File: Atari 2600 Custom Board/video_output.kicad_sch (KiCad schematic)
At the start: 0 parts

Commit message: Added buffer symbol and foot print
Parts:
- added U2: CD74HC4050M96, D16, symbol Atari2600_Library:CD74HC4050M96
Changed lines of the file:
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@@
 	(generator_version "8.0")
 	(paper "A4")
+	(symbol
+		(lib_id "Atari2600_Library:CD74HC4050M96")
+		(at 81.28 92.71 0)
+		(unit 1)
+		(exclude_from_sim no)
+		(in_bom yes)
+		(on_board yes)
+		(dnp no)
+		(fields_autoplaced yes)
+		(property "Reference" "U2"
+			(at 109.22 82.55 0)
+			(effects
+				(font
+					(size 1.524 1.524)
+				)
+			)
+		)
+		(property "Value" "CD74HC4050M96"
+			(at 109.22 85.09 0)
+			(effects
+				(font
+					(size 1.524 1.524)
+				)
+			)
+		)
+		(property "Footprint" "D16"
+			(at 81.28 92.71 0)
+			(effects
+				(font
+					(size 1.27 1.27)
+					(italic yes)
+				)
+				(hide yes)
+			)
+		)
+		(property "Datasheet" "CD74HC4050M96"
+			(at 81.28 92.71 0)
+			(effects
+				(font
+					(size 1.27 1.27)
+					(italic yes)
+				)
+				(hide yes)
+			)
+		)
+		(property "Description" ""
+			(at 81.28 92.71 0)
+			(effects
+				(font
+					(size 1.27 1.27)
+				)
+				(hide yes)
+			)
+		)
+		(pin "16"
+		)
+		(pin "15"
+		)
+		(pin "2"
+		)
+		(pin "12"
+		)
+		(pin "6"
+		)
+		(pin "8"
+		)
+		(pin "9"
+		)
+		(pin "4"
+		)
+		(pin "10"
+		)
+		(pin "14"
+		)
+		(pin "5"
+		)
+		(pin "7"
+		)
+		(pin "11"
+		)
+		(pin "1"
+		)
+		(pin "13"
+		)
+		(pin "3"
+		)
+		(instances
+			(project "atari2600"
+				(path "/d26a1e82-f8cb-48a3-8cce-edbb66ba228a/9cf3e399-02a1-4fa7-a3f8-062a21609052"
+					(reference "U2")
+					(unit 1)
+				)
+			)
+		)
+	)
 )

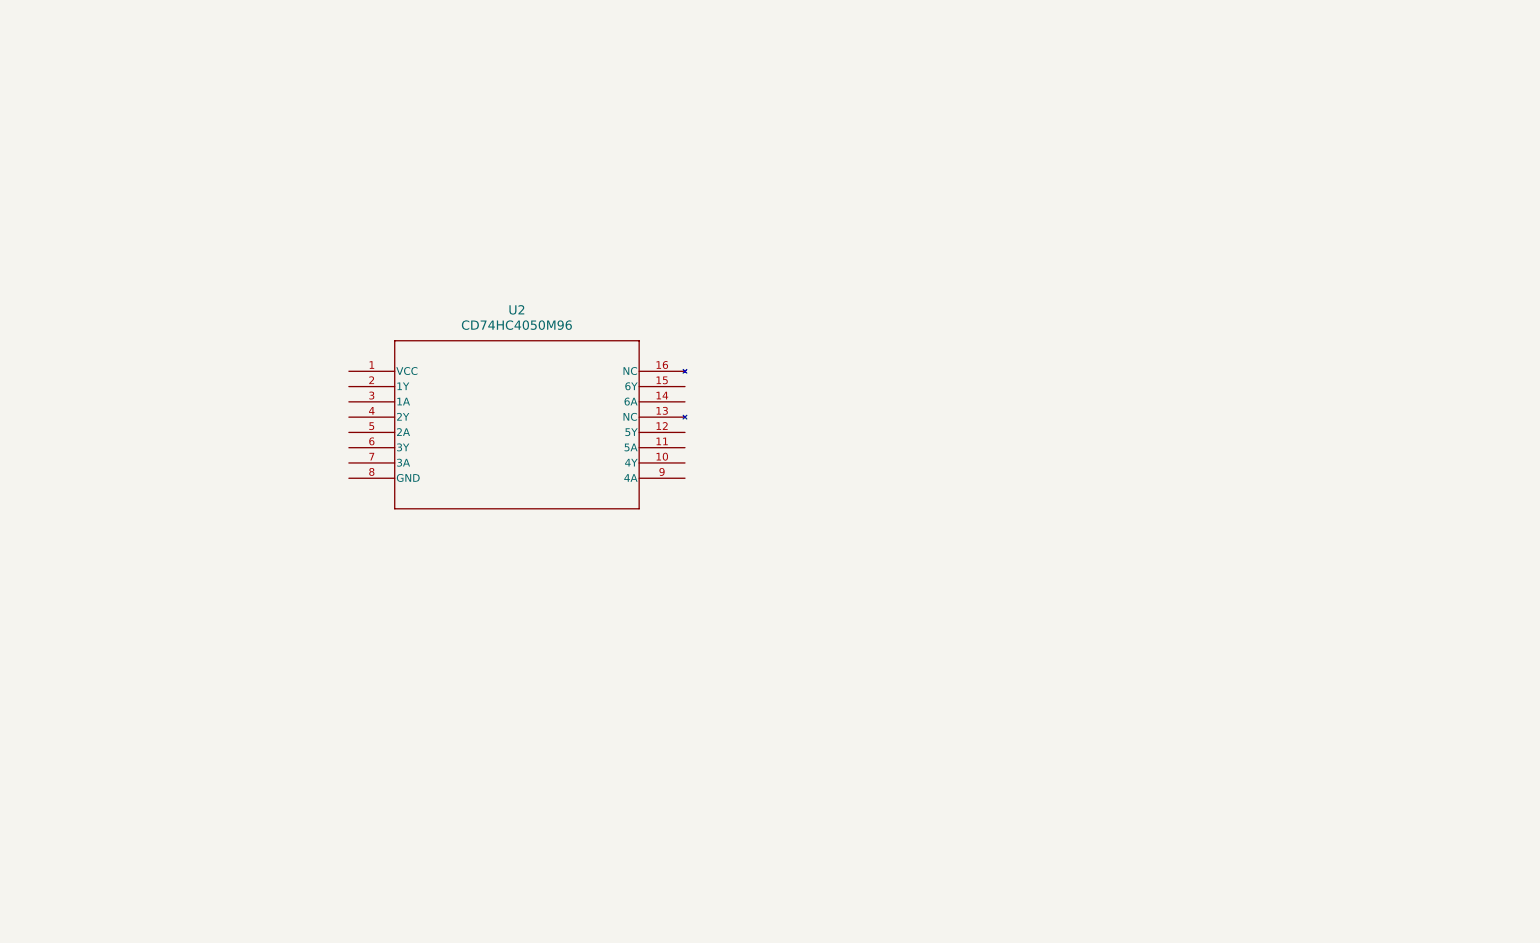
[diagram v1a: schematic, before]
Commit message: 1st pass of full schematic
1st pass of full schematic.  Need rules check and review.
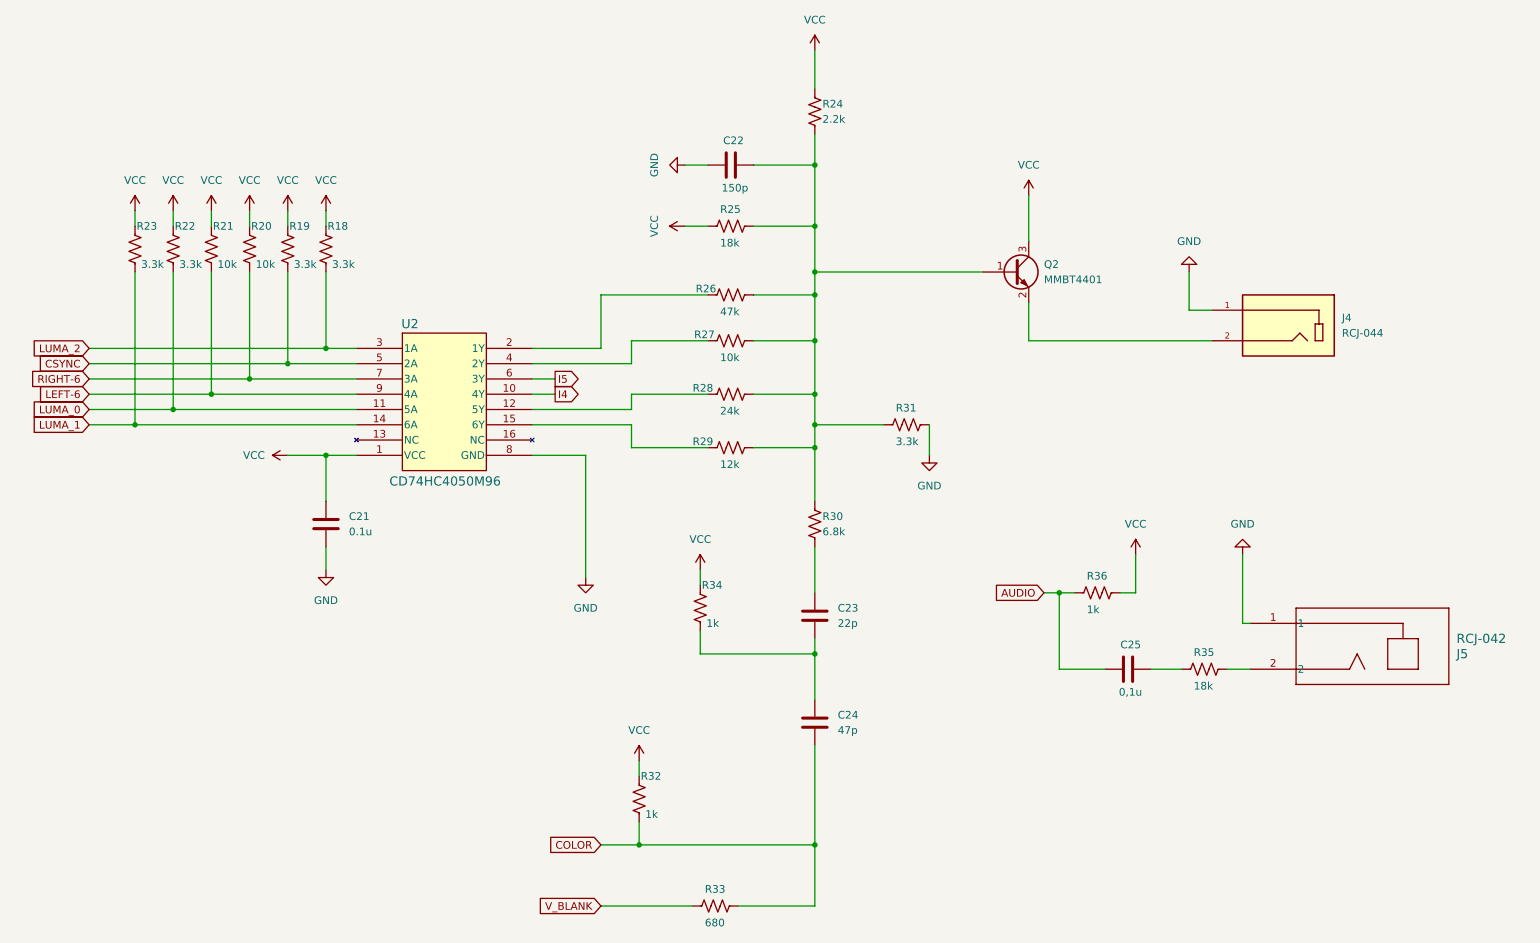
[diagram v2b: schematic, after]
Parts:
- added C21: 0.1u, symbol Device:C
- added C22: 150p, symbol Device:C
- added C23: 22p, symbol Device:C
- added C24: 47p, symbol Device:C
- added C25: 0,1u, symbol Device:C
- added J4: RCJ-044, RCJ-044:CUI_RCJ-044, symbol Atari2600_Library:RCJ-044
- added J5: RCJ-042, RCJ-042_CUD, symbol Atari2600_Library:RCJ-042
- added Q2: MMBT4401, symbol Device:Q_NPN_BEC
- added R18, R19, R22, R23, R31: 3.3k, symbol Device:R_US
- added R20, R21, R27: 10k, symbol Device:R_US
- added R24: 2.2k, symbol Device:R_US
- added R25, R35: 18k, symbol Device:R_US
- added R26: 47k, symbol Device:R_US
- added R28: 24k, symbol Device:R_US
- added R29: 12k, symbol Device:R_US
- added R30: 6.8k, symbol Device:R_US
- added R32, R34, R36: 1k, symbol Device:R_US
- added R33: 680, symbol Device:R_US
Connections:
- net VCC: now reaches U2.1 (VCC)
- net VCC: now also C21.1, Q2.3 (C), R18.1, R19.1, R20.1, R21.1, R22.1, R23.1, R24.1, R25.2, R32.1, R34.1, R36.1
- net I4: now reaches U2.10 (4Y)
- net LUMA_0: now reaches U2.11 (5A)
- net LUMA_0: now also R22.2
- net at U2.12 (5Y): now also R28.2
- net LUMA_1: now reaches U2.14 (6A)
- net LUMA_1: now also R23.2
- net at U2.15 (6Y): now also R29.2
- net at U2.2 (1Y): now also R26.2
- net LUMA_2: now reaches U2.3 (1A)
- net LUMA_2: now also R18.2
- net at U2.4 (2Y): now also R27.2
- net CSYNC: now reaches U2.5 (2A)
- net CSYNC: now also R19.2
- net I5: now reaches U2.6 (3Y)
- net RIGHT-6: now reaches U2.7 (3A)
- net RIGHT-6: now also R20.2
- net GND: now reaches U2.8 (GND)
- net GND: now also C21.2, C22.2, J4.1, J5.1, R31.1
- net LEFT-6: now reaches U2.9 (4A)
- net LEFT-6: now also R21.2
- new net: J4.2, Q2.2 (E)
- new net: C22.1, Q2.1 (B), R24.2, R25.1, R26.1, R27.1, R28.1, R29.1, R30.1, R31.2
- new net: J5.2, R35.1
- new net: C23.2, C24.1, R34.2
- new net: C25.1, R35.2
- new net: C23.1, R30.2
- new net AUDIO: C25.2, R36.2
- new net COLOR: C24.2, R32.2, R33.1
- new net V_BLANK: R33.2

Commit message: Fixed some incorrect values and re-annotated
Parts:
- renumbered C22 to C21, C21 to C22, C25 to C24, C24 to C25, R24 to R19, R25 to R20, R23 to R21, R21 to R23, R20 to R24, R19 to R25, R18 to R26, R26 to R27, R27 to R28, R28 to R29, R31 to R30, R29 to R31, R30 to R32, R36 to R33, R32 to R36, R33 to R37, U2 to U4

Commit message: assign footprints
assigned most footprints to schematic
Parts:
- C21, C22, C23, C24, C25: footprint (none) -> Capacitor_SMD:C_0805_2012Metric_Pad1.18x1.45mm_HandSolder
- J5: footprint RCJ-042_CUD -> Atari2600_Libary:RCJ-042_CUD
- Q2: footprint (none) -> Package_TO_SOT_SMD:TSOT-23
- R19, R20, R21, R22, R23, R24, R25, R26, R27, R28, R29, R30, R31, R32, R33, R34, R35, R36, R37: footprint (none) -> Resistor_SMD:R_0805_2012Metric_Pad1.20x1.40mm_HandSolder
- U4: footprint D16 -> Atari2600_Libary:CD74HC4050M96_16-SOIC_M
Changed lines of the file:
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@@
 			)
 		)
-		(property "Footprint" ""
+		(property "Footprint" "Resistor_SMD:R_0805_2012Metric_Pad1.20x1.40mm_HandSolder"
 			(at 144.526 97.536 90)
 			(effects
@@
 			)
 		)
-		(property "Footprint" "RCJ-042_CUD"
+		(property "Footprint" "Atari2600_Libary:RCJ-042_CUD"
 			(at 231.14 142.24 0)
 			(effects
@@
 			)
 		)
-		(property "Footprint" ""
+		(property "Footprint" "Capacitor_SMD:C_0805_2012Metric_Pad1.18x1.45mm_HandSolder"
 			(at 159.7152 154.94 0)
 			(effects
@@
 			)
 		)
-		(property "Footprint" ""
+		(property "Footprint" "Resistor_SMD:R_0805_2012Metric_Pad1.20x1.40mm_HandSolder"
 			(at 159.766 49.784 90)
 			(effects
@@
 			)
 		)
-		(property "Footprint" ""
+		(property "Footprint" "Resistor_SMD:R_0805_2012Metric_Pad1.20x1.40mm_HandSolder"
 			(at 144.526 106.426 90)
 			(effects
@@
 			)
 		)
-		(property "Footprint" ""
+		(property "Footprint" "Capacitor_SMD:C_0805_2012Metric_Pad1.18x1.45mm_HandSolder"
 			(at 207.01 143.2052 0)
 			(effects
@@
 			)
 		)
-		(property "Footprint" ""
+		(property "Footprint" "Resistor_SMD:R_0805_2012Metric_Pad1.20x1.40mm_HandSolder"
 			(at 78.486 72.644 90)
 			(effects
@@
 			)
 		)
-		(property "Footprint" ""
+		(property "Footprint" "Resistor_SMD:R_0805_2012Metric_Pad1.20x1.40mm_HandSolder"
 			(at 130.556 164.084 90)
 			(effects
@@
 			)
 		)
-		(property "Footprint" ""
+		(property "Footprint" "Capacitor_SMD:C_0805_2012Metric_Pad1.18x1.45mm_HandSolder"
 			(at 78.4352 121.92 0)
 			(effects
@@
 			)
 		)
-		(property "Footprint" ""
+		(property "Footprint" "Capacitor_SMD:C_0805_2012Metric_Pad1.18x1.45mm_HandSolder"
 			(at 159.7152 137.16 0)
 			(effects
@@
 			)
 		)
-		(property "Footprint" ""
+		(property "Footprint" "Resistor_SMD:R_0805_2012Metric_Pad1.20x1.40mm_HandSolder"
 			(at 144.526 88.646 90)
 			(effects
@@
 			)
 		)
-		(property "Footprint" ""
+		(property "Footprint" "Resistor_SMD:R_0805_2012Metric_Pad1.20x1.40mm_HandSolder"
 			(at 46.736 72.644 90)
 			(effects
@@
 			)
 		)
-		(property "Footprint" ""
+		(property "Footprint" "Resistor_SMD:R_0805_2012Metric_Pad1.20x1.40mm_HandSolder"
 			(at 65.786 72.644 90)
 			(effects
@@
 			)
 		)
-		(property "Footprint" ""
+		(property "Footprint" "Resistor_SMD:R_0805_2012Metric_Pad1.20x1.40mm_HandSolder"
 			(at 223.266 143.256 90)
 			(effects
@@
 			)
 		)
-		(property "Footprint" ""
+		(property "Footprint" "Resistor_SMD:R_0805_2012Metric_Pad1.20x1.40mm_HandSolder"
 			(at 205.486 130.556 90)
 			(effects
@@
 			)
 		)
-		(property "Footprint" ""
+		(property "Footprint" "Resistor_SMD:R_0805_2012Metric_Pad1.20x1.40mm_HandSolder"
 			(at 53.086 72.644 90)
 			(effects
@@
 			)
 		)
-		(property "Footprint" ""
+		(property "Footprint" "Package_TO_SOT_SMD:TSOT-23"
 			(at 196.85 73.66 0)
 			(effects
@@
 			)
 		)
-		(property "Footprint" ""
+		(property "Footprint" "Capacitor_SMD:C_0805_2012Metric_Pad1.18x1.45mm_HandSolder"
 			(at 140.97 59.3852 0)
 			(effects
@@
 			)
 		)
-		(property "Footprint" ""
+		(property "Footprint" "Resistor_SMD:R_0805_2012Metric_Pad1.20x1.40mm_HandSolder"
 			(at 141.986 182.626 90)
 			(effects
@@
 			)
 		)
-		(property "Footprint" ""
+		(property "Footprint" "Resistor_SMD:R_0805_2012Metric_Pad1.20x1.40mm_HandSolder"
 			(at 159.766 118.364 90)
 			(effects
@@
 			)
 		)
-		(property "Footprint" ""
+		(property "Footprint" "Resistor_SMD:R_0805_2012Metric_Pad1.20x1.40mm_HandSolder"
 			(at 144.526 81.026 90)
 			(effects
@@
 			)
 		)
-		(property "Footprint" ""
+		(property "Footprint" "Resistor_SMD:R_0805_2012Metric_Pad1.20x1.40mm_HandSolder"
 			(at 173.736 102.616 90)
 			(effects
@@
 			)
 		)
-		(property "Footprint" "D16"
+		(property "Footprint" "Atari2600_Libary:CD74HC4050M96_16-SOIC_M"
 			(at 90.17 86.36 0)
 			(effects
@@
 			)
 		)
-		(property "Footprint" ""
+		(property "Footprint" "Resistor_SMD:R_0805_2012Metric_Pad1.20x1.40mm_HandSolder"
 			(at 72.136 72.644 90)
 			(effects
@@
 			)
 		)
-		(property "Footprint" ""
+		(property "Footprint" "Resistor_SMD:R_0805_2012Metric_Pad1.20x1.40mm_HandSolder"
 			(at 140.716 132.334 90)
 			(effects
@@
 			)
 		)
-		(property "Footprint" ""
+		(property "Footprint" "Resistor_SMD:R_0805_2012Metric_Pad1.20x1.40mm_HandSolder"
 			(at 144.526 69.596 90)
 			(effects
@@
 			)
 		)
-		(property "Footprint" ""
+		(property "Footprint" "Resistor_SMD:R_0805_2012Metric_Pad1.20x1.40mm_HandSolder"
 			(at 59.436 72.644 90)
 			(effects

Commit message: Change footprintf to regular 0805
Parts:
- C21, C22, C23, C24, C25: footprint Capacitor_SMD:C_0805_2012Metric_Pad1.18x1.45mm_HandSolder -> Capacitor_SMD:C_0805_2012Metric
- R19, R20, R21, R22, R23, R24, R25, R26, R27, R28, R29, R30, R31, R32, R33, R34, R35, R36, R37: footprint Resistor_SMD:R_0805_2012Metric_Pad1.20x1.40mm_HandSolder -> Resistor_SMD:R_0805_2012Metric
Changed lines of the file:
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@@
 			)
 		)
-		(property "Footprint" "Resistor_SMD:R_0805_2012Metric_Pad1.20x1.40mm_HandSolder"
+		(property "Footprint" "Resistor_SMD:R_0805_2012Metric"
 			(at 144.526 97.536 90)
 			(effects
@@
 			)
 		)
-		(property "Footprint" "Capacitor_SMD:C_0805_2012Metric_Pad1.18x1.45mm_HandSolder"
+		(property "Footprint" "Capacitor_SMD:C_0805_2012Metric"
 			(at 159.7152 154.94 0)
 			(effects
@@
 			)
 		)
-		(property "Footprint" "Resistor_SMD:R_0805_2012Metric_Pad1.20x1.40mm_HandSolder"
+		(property "Footprint" "Resistor_SMD:R_0805_2012Metric"
 			(at 159.766 49.784 90)
 			(effects
@@
 			)
 		)
-		(property "Footprint" "Resistor_SMD:R_0805_2012Metric_Pad1.20x1.40mm_HandSolder"
+		(property "Footprint" "Resistor_SMD:R_0805_2012Metric"
 			(at 144.526 106.426 90)
 			(effects
@@
 			)
 		)
-		(property "Footprint" "Capacitor_SMD:C_0805_2012Metric_Pad1.18x1.45mm_HandSolder"
+		(property "Footprint" "Capacitor_SMD:C_0805_2012Metric"
 			(at 207.01 143.2052 0)
 			(effects
@@
 			)
 		)
-		(property "Footprint" "Resistor_SMD:R_0805_2012Metric_Pad1.20x1.40mm_HandSolder"
+		(property "Footprint" "Resistor_SMD:R_0805_2012Metric"
 			(at 78.486 72.644 90)
 			(effects
@@
 			)
 		)
-		(property "Footprint" "Resistor_SMD:R_0805_2012Metric_Pad1.20x1.40mm_HandSolder"
+		(property "Footprint" "Resistor_SMD:R_0805_2012Metric"
 			(at 130.556 164.084 90)
 			(effects
@@
 			)
 		)
-		(property "Footprint" "Capacitor_SMD:C_0805_2012Metric_Pad1.18x1.45mm_HandSolder"
+		(property "Footprint" "Capacitor_SMD:C_0805_2012Metric"
 			(at 78.4352 121.92 0)
 			(effects
@@
 			)
 		)
-		(property "Footprint" "Capacitor_SMD:C_0805_2012Metric_Pad1.18x1.45mm_HandSolder"
+		(property "Footprint" "Capacitor_SMD:C_0805_2012Metric"
 			(at 159.7152 137.16 0)
 			(effects
@@
 			)
 		)
-		(property "Footprint" "Resistor_SMD:R_0805_2012Metric_Pad1.20x1.40mm_HandSolder"
+		(property "Footprint" "Resistor_SMD:R_0805_2012Metric"
 			(at 144.526 88.646 90)
 			(effects
@@
 			)
 		)
-		(property "Footprint" "Resistor_SMD:R_0805_2012Metric_Pad1.20x1.40mm_HandSolder"
+		(property "Footprint" "Resistor_SMD:R_0805_2012Metric"
 			(at 46.736 72.644 90)
 			(effects
@@
 			)
 		)
-		(property "Footprint" "Resistor_SMD:R_0805_2012Metric_Pad1.20x1.40mm_HandSolder"
+		(property "Footprint" "Resistor_SMD:R_0805_2012Metric"
 			(at 65.786 72.644 90)
 			(effects
@@
 			)
 		)
-		(property "Footprint" "Resistor_SMD:R_0805_2012Metric_Pad1.20x1.40mm_HandSolder"
+		(property "Footprint" "Resistor_SMD:R_0805_2012Metric"
 			(at 223.266 143.256 90)
 			(effects
@@
 			)
 		)
-		(property "Footprint" "Resistor_SMD:R_0805_2012Metric_Pad1.20x1.40mm_HandSolder"
+		(property "Footprint" "Resistor_SMD:R_0805_2012Metric"
 			(at 205.486 130.556 90)
 			(effects
@@
 			)
 		)
-		(property "Footprint" "Resistor_SMD:R_0805_2012Metric_Pad1.20x1.40mm_HandSolder"
+		(property "Footprint" "Resistor_SMD:R_0805_2012Metric"
 			(at 53.086 72.644 90)
 			(effects
@@
 			)
 		)
-		(property "Footprint" "Capacitor_SMD:C_0805_2012Metric_Pad1.18x1.45mm_HandSolder"
+		(property "Footprint" "Capacitor_SMD:C_0805_2012Metric"
 			(at 140.97 59.3852 0)
 			(effects
@@
 			)
 		)
-		(property "Footprint" "Resistor_SMD:R_0805_2012Metric_Pad1.20x1.40mm_HandSolder"
+		(property "Footprint" "Resistor_SMD:R_0805_2012Metric"
 			(at 141.986 182.626 90)
 			(effects
@@
 			)
 		)
-		(property "Footprint" "Resistor_SMD:R_0805_2012Metric_Pad1.20x1.40mm_HandSolder"
+		(property "Footprint" "Resistor_SMD:R_0805_2012Metric"
 			(at 159.766 118.364 90)
 			(effects
@@
 			)
 		)
-		(property "Footprint" "Resistor_SMD:R_0805_2012Metric_Pad1.20x1.40mm_HandSolder"
+		(property "Footprint" "Resistor_SMD:R_0805_2012Metric"
 			(at 144.526 81.026 90)
 			(effects
@@
 			)
 		)
-		(property "Footprint" "Resistor_SMD:R_0805_2012Metric_Pad1.20x1.40mm_HandSolder"
+		(property "Footprint" "Resistor_SMD:R_0805_2012Metric"
 			(at 173.736 102.616 90)
 			(effects
@@
 			)
 		)
-		(property "Footprint" "Resistor_SMD:R_0805_2012Metric_Pad1.20x1.40mm_HandSolder"
+		(property "Footprint" "Resistor_SMD:R_0805_2012Metric"
 			(at 72.136 72.644 90)
 			(effects
@@
 			)
 		)
-		(property "Footprint" "Resistor_SMD:R_0805_2012Metric_Pad1.20x1.40mm_HandSolder"
+		(property "Footprint" "Resistor_SMD:R_0805_2012Metric"
 			(at 140.716 132.334 90)
 			(effects
@@
 			)
 		)
-		(property "Footprint" "Resistor_SMD:R_0805_2012Metric_Pad1.20x1.40mm_HandSolder"
+		(property "Footprint" "Resistor_SMD:R_0805_2012Metric"
 			(at 144.526 69.596 90)
 			(effects
@@
 			)
 		)
-		(property "Footprint" "Resistor_SMD:R_0805_2012Metric_Pad1.20x1.40mm_HandSolder"
+		(property "Footprint" "Resistor_SMD:R_0805_2012Metric"
 			(at 59.436 72.644 90)
 			(effects
